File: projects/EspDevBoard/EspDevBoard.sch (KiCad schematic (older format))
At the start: 29 parts

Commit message: working on EspDevBoard
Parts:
- added C? (x3): 100nF, symbol C
- added D?: DIODE, symbol DIODE
- added R? (x2): 0.1R 1%, symbol R
- added R? (x4): 10R, symbol R
- added R?: 10K, symbol R
- added R?: 330R, symbol R
- added R?: 1K, symbol R
- added S?: User button, TACTILE, symbol TAC_SWITCH
- added U?: AP1117, symbol AP1117
- added X?: Resonator, symbol Resonator
- S?: value TAC_SWITCH -> Reset
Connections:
- net +3.3V: now also U?.14 (VCC), C?.1, D?.2 (K), R?.1, R?.2
- net A_Reset: now also S?.3, S?.4, D?.1 (A), R?.1
- net GND: now also S?.1, S?.2, C?.2, R?.2, S?.3, S?.4, U?.1 (GND), X?.2 (GND)
- net SCL: now also U?.18 ((OC0B/SCL/INT0)PD0)
- net SDA: now also U?.19 ((SDA/INT1)PD1)
- net Vin+: now also C?.1, R?.1, R?.2; no longer U?.1 (Vin+)
- net Vin-: now also C?.2, R?.1, R?.1; no longer U?.2 (Vin-)
- net Vout+: now also C?.1, R?.1, R?.2; no longer U?.1 (Vin+)
- net Vout-: now also C?.2, R?.1, R?.1; no longer U?.2 (Vin-)
- net at U?.16 (XTAL2): now also X?.3 (X2)
- net at U?.17 (XTAL1): now also X?.1 (X1)
- net A_RX: now reaches U?.20 ((RXD1/INT2)PD2)
- net A_RX: now also U?.26 (TX)
- net A_TX: now reaches U?.21 ((TXD1/INT3)PD3)
- net A_TX: now also U?.24 (RX)
- net D5: now reaches U?.31 (PC6(OC3A/^OC4A))
- net D5: now also R?.2, S?.1, S?.2
- net IO_13: now reaches U?.32 (PC7(ICP3/CLK0/OC4A)
- net IO_13: now also D?.1 (A)
- net at D?.2 (K): now also R?.1
- new net: R?.2, U?.1 (Vin+) (x2)
- new net: R?.2, U?.2 (Vin-) (x2)
- no-connect marks 11 -> 14
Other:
- moved on the sheet: D?, R?, S?, U?

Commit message: work on EspDevBoard
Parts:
- added C? (x2): 4u7F, symbol C
- added R? (x5): 10K, symbol R
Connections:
- net Reset is gone; now on net ESP_Reset: U?.25 (RST), U?.7 (!Reset)
- net +3.3V: now also P?.2, U?.17 (CLK), U?.2 (VO), U?.8 (VCC), C?.1, R?.1, R?.1, R?.1, R?.1
- net A_RX: now also U?.16 (TXD0)
- net A_TX: now also U?.15 (RXD0)
- net CS: now also U?.10 (D4), U?.11 (GPIO2), R?.2; no longer U?.22 (D8)
- net En+: now also U?.10 (GPIO15), U?.22 (D8), R?.2; no longer U?.18 (D6)
- net GND: now also P?.19 (P19), U?.15 (SDO), U?.9 (GND), C?.2, C?.2, R?.1
- net MOSI: now also U?.7 (GPIO13)
- net RES: now also U?.2 (D0), U?.4 (GPIO16); no longer U?.10 (D4)
- net RS: now also U?.18 (D6), U?.6 (GPIO12); no longer U?.8 (D3)
- net SCL: now also U?.14 (GPIO5)
- net SCLK: now also U?.5 (GPIO14)
- net SDA: now also U?.13 (GPIO4)
- net USB_5V: now also JP?.2, U?.3 (VI), C?.1
- net Vdd: no longer JP?.2, P?.2
- net ESP_Reset: now reaches U?.1 (RST)
- net ESP_Reset: now also U?.29 (PB5(PCINT5/OC1A/^OC4B/ADC12)), R?.2
- net BootMode: now reaches U?.12 (GPIO0)
- net BootMode: now also U?.28 (PB4(PCINT4/ADC11)), U?.8 (D3), R?.2
- net ESP_En: now reaches U?.3 (EN)
- net ESP_En: now also U?.23 (EN), R?.2
- removed net PS: P?.19 (P19), U?.2 (D0)
- no-connect marks 14 -> 32
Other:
- note added: "A0"
- note added: "A1"
- note added: "A2"
- note added: "A3"
- note added: "A4"
- note added: "A5"
- note added: "D0"
- note added: "D1"
- note added: "D10"
- note added: "D12"
- note added: "D2"
- note added: "D3"
- note added: "D4"
- note added: "D6"
- note added: "D7"
- note added: "D8"
- note added: "D9"
- note added: "RXLED"
- note added: "TXLED"
- moved on the sheet: JP?, U?

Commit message: EDB schematic done
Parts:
- added JP2: JUMPER3, symbol JUMPER3
- gave numbers to parts that had none: 52
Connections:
- net Vdd is gone; now on net +3.3V: U2.29 (Vin)
- net GND: now also R15.2; no longer R15.1
- net USB_5V: now also JP2.3; no longer C1.1, JP1.2, U3.3 (VI)
- net D-: now reaches R1.1, U5.3 (D-)
- net at U5.33 (PE2(^HWB)): now also R15.1; no longer R15.2
- net D+: now reaches R2.1, U5.4 (D+)
- net ICSP_Power: now reaches P1.2
- net ICSP_Power: now also JP2.1
- net En: no longer names the net of P4.13 (P13)
- net IO_13: no longer names the net of D2.1 (A), U5.32 (PC7(ICP3/CLK0/OC4A)
- new net: C1.1, JP1.2, JP2.2, U3.3 (VI)
- no-connect marks 32 -> 33
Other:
- note added: "32u4 based Arduino"
- note added: "En"
- note added: "ICSP 32u4"
- note added: "IO_11"
- note added: "NodeMCU / ESP8266 module"
- note added: "Powersupply"
- note added: "SEPIC interface"
- note added: "Sepic module"
- note added: "USB"
- note added: "nhd-1.69-160128UGC3"
- note removed: "Sepic"
- moved on the sheet: C1, C10, C11, C12, C13, C2, C3, C4, C5, C6, C7, C8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

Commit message: update pdf
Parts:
- U6, U7: symbol INA219_SOT23_8 -> INA219_SOT23_8-RESCUE-EspDevBoard
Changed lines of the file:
@@
 EESchema Schematic File Version 2
+LIBS:EspDevBoard-rescue
 LIBS:power
 LIBS:device
@@
 $EndComp
 $Comp
-L INA219_SOT23_8 U6
+L INA219_SOT23_8-RESCUE-EspDevBoard U6
 U 1 1 56957ADD
 P 8600 4400
@@
 $EndComp
 $Comp
-L INA219_SOT23_8 U7
+L INA219_SOT23_8-RESCUE-EspDevBoard U7
 U 1 1 56957B3E
 P 8600 5600

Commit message: netlist created
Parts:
- removed U6: INA219_SOT23_Vin, symbol INA219_SOT23_8-RESCUE-EspDevBoard
- removed U7: INA219_SOT23_Vout, symbol INA219_SOT23_8-RESCUE-EspDevBoard
- added U6, U7: INA219_SOT23_8, symbol INA219_SOT23_8
- S1, S2: footprint TACTILE -> (none)
- U5: footprint MODULE -> (none)
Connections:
- net +3.3V: now also U6.4 (Vs), U6.7 (A0), U6.8 (A1), U7.4 (Vs)
- net GND: now also U6.3 (GND), U7.3 (GND), U7.7 (A0), U7.8 (A1)
- net SCL: now also U6.5 (SCL), U7.5 (SCL)
- net SDA: now also U6.6 (SDA), U7.6 (SDA)
- net at R11.2: now also U6.1 (Vin+)
- net at R12.2: now also U6.2 (Vin-)
- net at R13.2: now also U7.1 (Vin+)
- net at R14.2: now also U7.2 (Vin-)

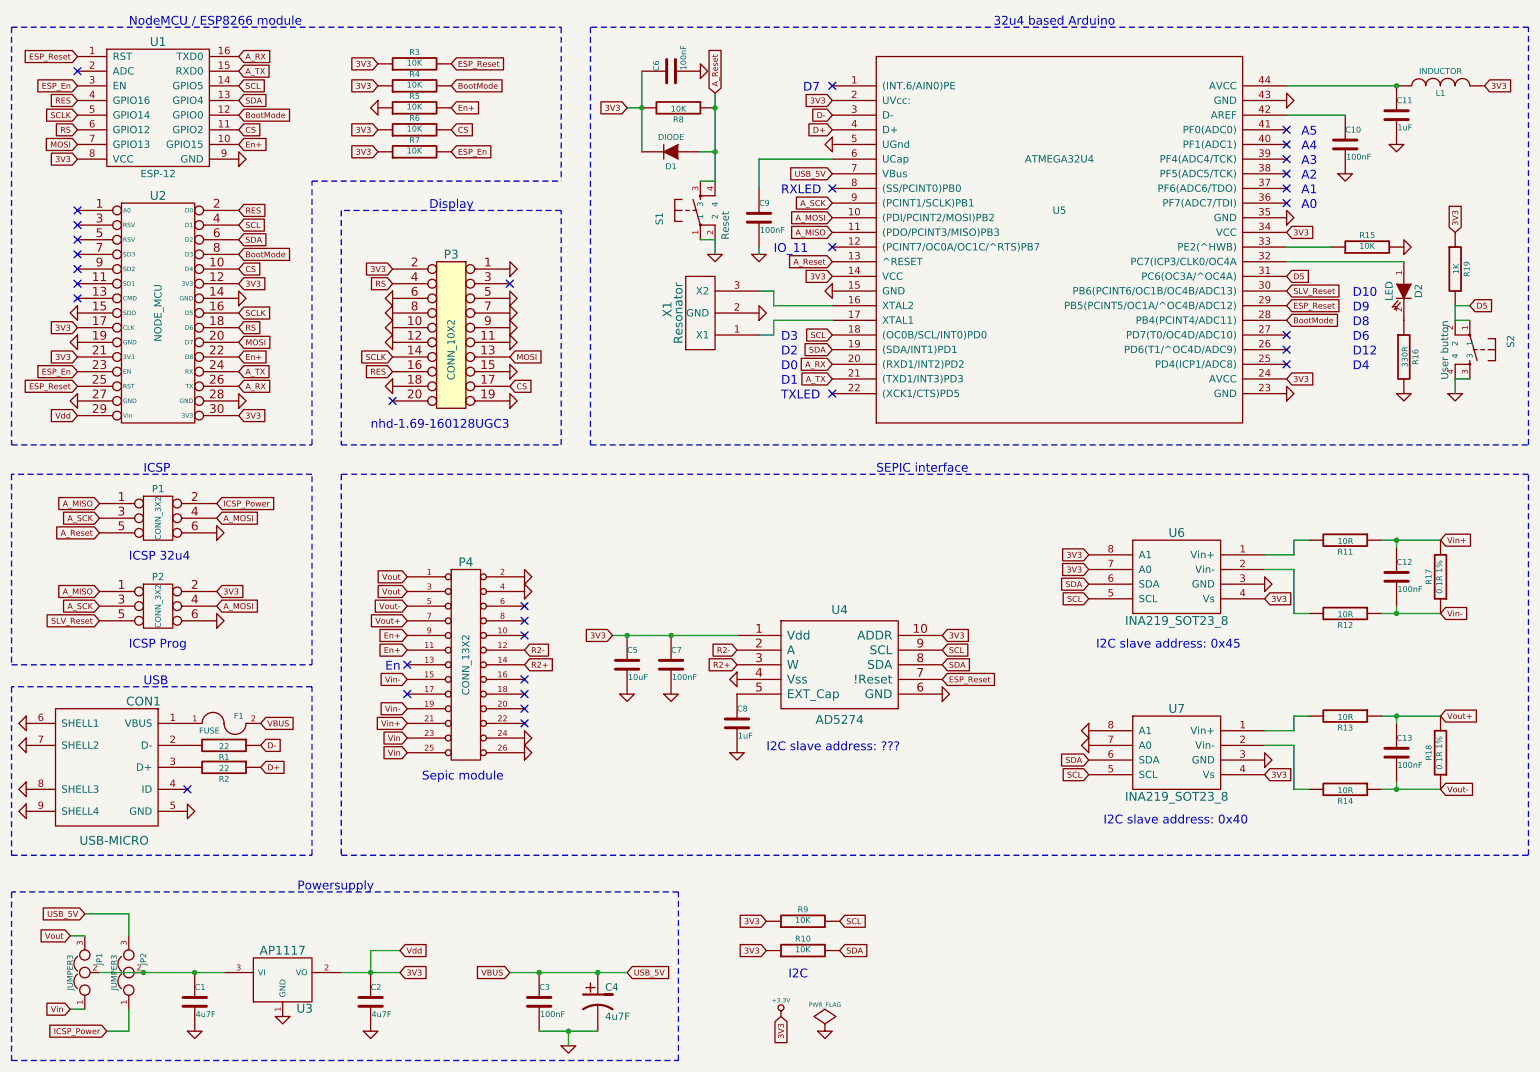
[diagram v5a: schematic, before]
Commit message: changing esp-12
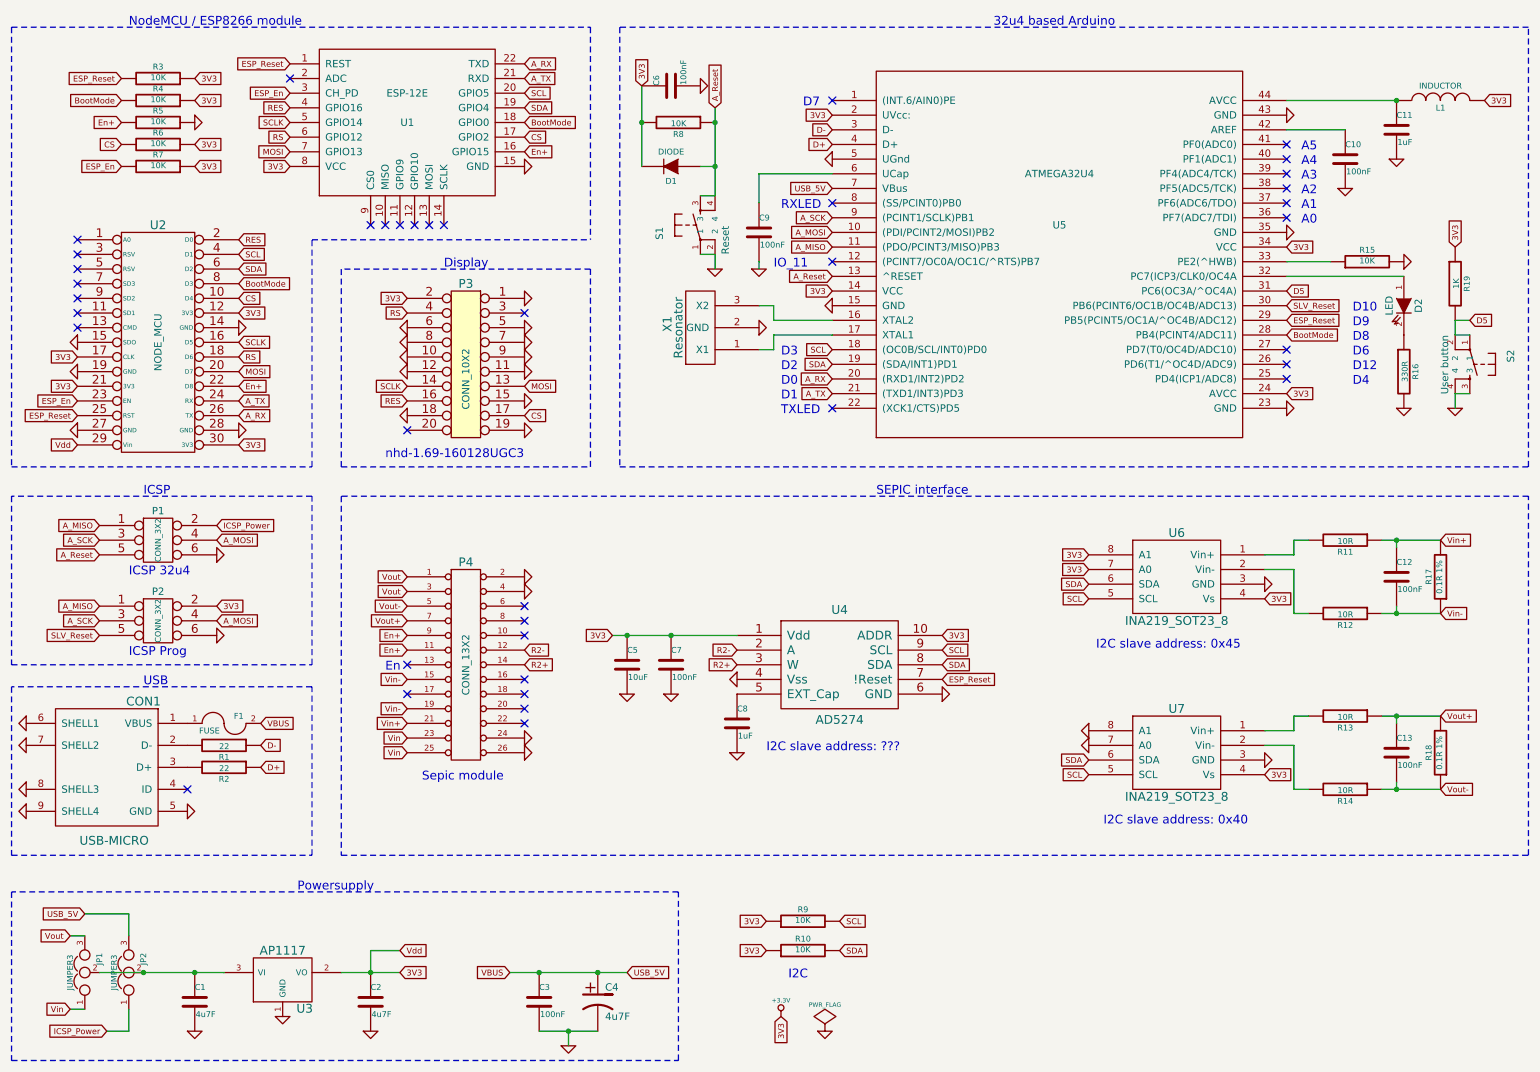
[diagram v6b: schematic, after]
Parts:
- removed U1: ESP-12, symbol ESP-12
- added U1: ESP-12E, symbol ESP-12E
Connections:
- net +3.3V: now also U1.8 (VCC)
- net A_RX: now also U1.22 (TXD)
- net A_TX: now also U1.21 (RXD)
- net BootMode: now also U1.18 (GPIO0)
- net CS: now also U1.17 (GPIO2)
- net ESP_En: now also U1.3 (CH_PD)
- net ESP_Reset: now also U1.1 (REST)
- net En+: now also U1.16 (GPIO15)
- net GND: now also U1.15 (GND)
- net MOSI: now also U1.7 (GPIO13)
- net RES: now also U1.4 (GPIO16)
- net RS: now also U1.6 (GPIO12)
- net SCL: now also U1.20 (GPIO5)
- net SCLK: now also U1.5 (GPIO14)
- net SDA: now also U1.19 (GPIO4)
- no-connect marks 33 -> 39
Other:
- moved on the sheet: C10, C11, C6, C9, D1, D2, L1, P1, P2, P3, R15, R16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

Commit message: new footprint
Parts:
- CON1: footprint (none) -> frep:USB_Micro
- D1: footprint (none) -> frep:Diode-MiniMELF_Handsoldering
- D2: footprint (none) -> frep:LED-0805
- R1, R2: value 22 -> 33; footprint (none) -> frep:R0805
- R10, R11, R12, R13, R14, R15, R16, R19, R3, R4, R5, R6, R7, R8, R9: footprint (none) -> frep:R0805
- S1, S2: footprint (none) -> frep:TACTILE-PTH
- U1: footprint (none) -> frep:ESP-12E
- U5: footprint (none) -> frep:TQFP44
- U6, U7: footprint (none) -> frep:SOT-23-8
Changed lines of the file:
@@
 F 0 "U5" H 7800 2400 50  0000 C CNN
 F 1 "ATMEGA32U4" H 7800 2750 50  0000 C CNN
-F 2 "" H 7800 2650 50  0001 C CNN
+F 2 "frep:TQFP44" H 7800 2650 50  0001 C CNN
 F 3 "DOCUMENTATION" H 7800 2550 50  0001 C CNN
 	1    7800 2200
@@
 F 0 "R9" V 6130 6750 40  0000 C CNN
 F 1 "10K" V 6057 6751 40  0000 C CNN
-F 2 "" V 5980 6750 30  0001 C CNN
+F 2 "frep:R0805" V 5980 6750 30  0001 C CNN
 F 3 "" H 6050 6750 30  0000 C CNN
 	1    6050 6750
@@
 F 0 "R10" V 6130 6950 40  0000 C CNN
 F 1 "10K" V 6057 6951 40  0000 C CNN
-F 2 "" V 5980 6950 30  0001 C CNN
+F 2 "frep:R0805" V 5980 6950 30  0001 C CNN
 F 3 "" H 6050 6950 30  0000 C CNN
 	1    6050 6950
@@
 F 0 "CON1" H 1050 6150 60  0000 C CNN
 F 1 "USB-MICRO" H 1250 5200 60  0000 C CNN
-F 2 "" H 1300 5700 60  0001 C CNN
+F 2 "frep:USB_Micro" H 1300 5700 60  0001 C CNN
 F 3 "" H 1300 5700 60  0000 C CNN
 	1    1300 5700
@@
 P 2100 5550
 F 0 "R1" V 2180 5550 40  0000 C CNN
-F 1 "22" V 2107 5551 40  0000 C CNN
-F 2 "" V 2030 5550 30  0001 C CNN
+F 1 "33" V 2107 5551 40  0000 C CNN
+F 2 "frep:R0805" V 2030 5550 30  0001 C CNN
 F 3 "" H 2100 5550 30  0000 C CNN
 	1    2100 5550
@@
 P 2100 5700
 F 0 "R2" V 2180 5700 40  0000 C CNN
-F 1 "22" V 2107 5701 40  0000 C CNN
-F 2 "" V 2030 5700 30  0001 C CNN
+F 1 "33" V 2107 5701 40  0000 C CNN
+F 2 "frep:R0805" V 2030 5700 30  0001 C CNN
 F 3 "" H 2100 5700 30  0000 C CNN
 	1    2100 5700
@@
 F 0 "R15" V 9980 2250 40  0000 C CNN
 F 1 "10K" V 9907 2251 40  0000 C CNN
-F 2 "" V 9830 2250 30  0001 C CNN
+F 2 "frep:R0805" V 9830 2250 30  0001 C CNN
 F 3 "" H 9900 2250 30  0000 C CNN
 	1    9900 2250
@@
 F 0 "S1" H 5250 2250 50  0000 L BNN
 F 1 "Reset" H 5150 1800 50  0000 L BNN
-F 2 "" H 5350 2150 50  0001 C CNN
+F 2 "frep:TACTILE-PTH" H 5350 2150 50  0001 C CNN
 F 3 "" H 5350 2000 60  0000 C CNN
 	1    5350 2000
@@
 F 0 "D2" H 10150 2650 50  0000 C CNN
 F 1 "LED" H 10150 2450 50  0000 C CNN
-F 2 "" H 10150 2550 60  0001 C CNN
+F 2 "frep:LED-0805" H 10150 2550 60  0001 C CNN
 F 3 "" H 10150 2550 60  0000 C CNN
 	1    10150 2550
@@
 F 0 "R11" V 9830 4150 40  0000 C CNN
 F 1 "10R" V 9757 4151 40  0000 C CNN
-F 2 "" V 9680 4150 30  0001 C CNN
+F 2 "frep:R0805" V 9680 4150 30  0001 C CNN
 F 3 "" H 9750 4150 30  0000 C CNN
 	1    9750 4150
@@
 F 0 "R12" V 9830 4650 40  0000 C CNN
 F 1 "10R" V 9757 4651 40  0000 C CNN
-F 2 "" V 9680 4650 30  0001 C CNN
+F 2 "frep:R0805" V 9680 4650 30  0001 C CNN
 F 3 "" H 9750 4650 30  0000 C CNN
 	1    9750 4650
@@
 F 0 "R13" V 9830 5350 40  0000 C CNN
 F 1 "10R" V 9757 5351 40  0000 C CNN
-F 2 "" V 9680 5350 30  0001 C CNN
+F 2 "frep:R0805" V 9680 5350 30  0001 C CNN
 F 3 "" H 9750 5350 30  0000 C CNN
 	1    9750 5350
@@
 F 0 "R14" V 9830 5850 40  0000 C CNN
 F 1 "10R" V 9757 5851 40  0000 C CNN
-F 2 "" V 9680 5850 30  0001 C CNN
+F 2 "frep:R0805" V 9680 5850 30  0001 C CNN
 F 3 "" H 9750 5850 30  0000 C CNN
 	1    9750 5850
@@
 F 0 "S2" H 10500 3200 50  0000 L BNN
 F 1 "User button" H 10400 2750 50  0000 L BNN
-F 2 "" H 10600 3100 50  0001 C CNN
+F 2 "frep:TACTILE-PTH" H 10600 3100 50  0001 C CNN
 F 3 "" H 10600 2950 60  0000 C CNN
 	1    10600 2950
@@
 F 0 "D1" H 5150 1700 40  0000 C CNN
 F 1 "DIODE" H 5150 1500 40  0000 C CNN
-F 2 "" H 5150 1600 60  0001 C CNN
+F 2 "frep:Diode-MiniMELF_Handsoldering" H 5150 1600 60  0001 C CNN
 F 3 "" H 5150 1600 60  0000 C CNN
 	1    5150 1600
@@
 F 0 "R8" V 5280 1300 40  0000 C CNN
 F 1 "10K" V 5207 1301 40  0000 C CNN
-F 2 "" V 5130 1300 30  0001 C CNN
+F 2 "frep:R0805" V 5130 1300 30  0001 C CNN
 F 3 "" H 5200 1300 30  0000 C CNN
 	1    5200 1300
@@
 F 0 "R16" V 10230 3000 40  0000 C CNN
 F 1 "330R" V 10157 3001 40  0000 C CNN
-F 2 "" V 10080 3000 30  0001 C CNN
+F 2 "frep:R0805" V 10080 3000 30  0001 C CNN
 F 3 "" H 10150 3000 30  0000 C CNN
 	1    10150 3000
@@
 F 0 "R19" V 10580 2400 40  0000 C CNN
 F 1 "1K" V 10507 2401 40  0000 C CNN
-F 2 "" V 10430 2400 30  0001 C CNN
+F 2 "frep:R0805" V 10430 2400 30  0001 C CNN
 F 3 "" H 10500 2400 30  0000 C CNN
 	1    10500 2400
@@
 F 0 "R7" V 1730 1600 40  0000 C CNN
 F 1 "10K" V 1657 1601 40  0000 C CNN
-F 2 "" V 1580 1600 30  0001 C CNN
+F 2 "frep:R0805" V 1580 1600 30  0001 C CNN
 F 3 "" H 1650 1600 30  0000 C CNN
 	1    1650 1600
@@
 F 0 "R6" V 1730 1450 40  0000 C CNN
 F 1 "10K" V 1657 1451 40  0000 C CNN
-F 2 "" V 1580 1450 30  0001 C CNN
+F 2 "frep:R0805" V 1580 1450 30  0001 C CNN
 F 3 "" H 1650 1450 30  0000 C CNN
 	1    1650 1450
@@
 F 0 "R5" V 1730 1300 40  0000 C CNN
 F 1 "10K" V 1657 1301 40  0000 C CNN
-F 2 "" V 1580 1300 30  0001 C CNN
+F 2 "frep:R0805" V 1580 1300 30  0001 C CNN
 F 3 "" H 1650 1300 30  0000 C CNN
 	1    1650 1300
@@
 F 0 "R4" V 1730 1150 40  0000 C CNN
 F 1 "10K" V 1657 1151 40  0000 C CNN
-F 2 "" V 1580 1150 30  0001 C CNN
+F 2 "frep:R0805" V 1580 1150 30  0001 C CNN
 F 3 "" H 1650 1150 30  0000 C CNN
 	1    1650 1150
@@
 F 0 "R3" V 1730 1000 40  0000 C CNN
 F 1 "10K" V 1657 1001 40  0000 C CNN
-F 2 "" V 1580 1000 30  0001 C CNN
+F 2 "frep:R0805" V 1580 1000 30  0001 C CNN
 F 3 "" H 1650 1000 30  0000 C CNN
 	1    1650 1000
@@
 F 0 "U6" H 8600 4700 60  0000 C CNN
 F 1 "INA219_SOT23_8" H 8600 4100 60  0000 C CNN
-F 2 "" H 8600 4200 60  0001 C CNN
+F 2 "frep:SOT-23-8" H 8600 4200 60  0001 C CNN
 F 3 "" H 8600 4200 60  0000 C CNN
 	1    8600 4400
@@
 F 0 "U7" H 8600 5900 60  0000 C CNN
 F 1 "INA219_SOT23_8" H 8600 5300 60  0000 C CNN
-F 2 "" H 8600 5400 60  0001 C CNN
+F 2 "frep:SOT-23-8" H 8600 5400 60  0001 C CNN
 F 3 "" H 8600 5400 60  0000 C CNN
 	1    8600 5600
@@
 F 0 "U1" H 3350 1100 50  0000 C CNN
 F 1 "ESP-12E" H 3350 1300 50  0000 C CNN
-F 2 "" H 3350 1200 50  0001 C CNN
+F 2 "frep:ESP-12E" H 3350 1200 50  0001 C CNN
 F 3 "" H 3350 1200 50  0001 C CNN
 	1    3350 1200
